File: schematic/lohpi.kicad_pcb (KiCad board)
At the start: 2 copper layers, 0 parts

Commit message: Schematic capture almost done. RF layout started.
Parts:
- added C1: 10uF, Capacitors_SMD:C_0603, F.Cu at (222.2, 74.6)
- added C10: 4.7uF, Capacitors_SMD:C_0603, F.Cu at (226.7, 74.6)
- added C11: 4.7uF, Capacitors_SMD:C_0603, F.Cu at (219.8, 79.6)
- added C12: 4.7uF, Capacitors_SMD:C_0603, F.Cu at (231.4, 69.5)
- added C13: 10nF, Capacitors_SMD:C_0603, F.Cu at (215.3, 86.0)
- added C14: 1.0uF, Capacitors_SMD:C_0603, F.Cu at (219.7, 86.0)
- added C15: 1.0uF, Capacitors_SMD:C_0603, F.Cu at (215.3, 91.1)
- added C16: 1.0uF, Capacitors_SMD:C_0603, F.Cu at (236.1, 69.5)
- added C17: 1.0uF, Capacitors_SMD:C_0603, F.Cu at (231.4, 74.6)
- added C18: 56pF, Capacitors_SMD:C_0603, F.Cu at (200.1, -37.2)
- added C19: 56pF, Capacitors_SMD:C_0603, F.Cu at (163.5, -0.87)
- added C2: 4.7uF, Capacitors_SMD:C_0603, F.Cu at (210.7, 91.1)
- added C20: 56pF, Capacitors_SMD:C_0603, F.Cu at (168.7, -5.92)
- added C21: 56pF, Capacitors_SMD:C_0603, F.Cu at (184.3, -23.1)
- added C22: 56pF, Capacitors_SMD:C_0603, F.Cu at (174.3, -11.0)
- added C23: 56pF, Capacitors_SMD:C_0603, F.Cu at (158.9, 4.18)
- added C24: 1.0uF, Capacitors_SMD:C_0603, F.Cu at (190.2, -30.1)
- added C25: 100nF, Capacitors_SMD:C_0603, F.Cu at (159.3, -16.0)
- added C26: 100nF, Capacitors_SMD:C_0603, F.Cu at (179.7, -23.1)
- added C27: 100nF, Capacitors_SMD:C_0603, F.Cu at (174.8, -16.0)
- added C28: 100nF, Capacitors_SMD:C_0603, F.Cu at (164.5, -16.0)
- added C29: 100nF, Capacitors_SMD:C_0603, F.Cu at (169.7, -16.0)
- added C3: 0.1uF, Capacitors_SMD:C_0603, F.Cu at (206.0, 91.7)
- added C30: 1.0uF, Capacitors_SMD:C_0603, F.Cu at (159.1, -0.87)
- added C31: 100nF, Capacitors_SMD:C_0603, F.Cu at (159.3, -5.92)
- added C32: 100nF, Capacitors_SMD:C_0603, F.Cu at (169.7, -11.0)
- added C33: 100nF, Capacitors_SMD:C_0603, F.Cu at (164.5, -11.0)
- added C34: 1uF, Capacitors_SMD:C_0402, F.Cu at (218.0, 125.9)
- added C35: 1uF, Capacitors_SMD:C_0402, F.Cu at (221.9, 121.3)
- added C36: 100nF, Capacitors_SMD:C_0603, F.Cu at (159.3, -11.0)
- added C37: 4.7uF, Capacitors_SMD:C_0603, F.Cu at (164.3, -5.92)
- added C38: 1nF, Capacitors_SMD:C_0402, F.Cu at (230.3, 111.8)
- added C39: 100nF, Capacitors_SMD:C_0402, F.Cu at (194.9, 116.4)
- added C4: 1nF, Capacitors_SMD:C_0603, F.Cu at (211.5, 86.0)
- added C40: 100nF, Capacitors_SMD:C_0402, F.Cu at (200.1, 107.3)
- added C41: 100nF, Capacitors_SMD:C_0402, F.Cu at (188.5, 126.4)
- added C42: 100nF, Capacitors_SMD:C_0402, F.Cu at (194.9, 111.8)
- added C43: 10nF, Capacitors_SMD:C_0402, F.Cu at (235.6, 102.7)
- added C44: 10nF, Capacitors_SMD:C_0402, F.Cu at (226.5, 111.8)
- added C45: 1uF, Capacitors_SMD:C_0402, F.Cu at (218.4, 121.3)
- added C46: 100nF, Capacitors_SMD:C_0402, F.Cu at (207.2, 102.7)
- added C47: 1uF, Capacitors_SMD:C_0402, F.Cu at (233.1, 107.3)
- added C48: 100nF, Capacitors_SMD:C_0402, F.Cu at (138.3, 153.7)
- added C49: 1uF, Capacitors_SMD:C_0402, F.Cu at (214.4, 126.3)
- added C5: 4.7uF, Capacitors_SMD:C_0603, F.Cu at (206.0, 86.6)
- added C50: 1uF, Capacitors_SMD:C_0402, F.Cu at (229.7, 107.3)
- added C51: DNP, Capacitors_SMD:C_0402, F.Cu at (142.1, 156.8)
- added C52: DNP, Capacitors_SMD:C_0402, F.Cu at (144.7, 156.8)
- added C53: 56pF, Capacitors_SMD:C_0402, F.Cu at (139.6, 160.9)
- added C54: 56pF, Capacitors_SMD:C_0402, F.Cu at (125.7, 153.5)
- added C55: 5.9pF, Capacitors_SMD:C_0402, F.Cu at (123.4, 154.2)
- added C56: 56pF, Capacitors_SMD:C_0402, F.Cu at (129.3, 162.2)
- added C57: DNP, Capacitors_SMD:C_0402, F.Cu at (128.3, 163.8)
- added C58: 56pF, Capacitors_SMD:C_0402, F.Cu at (112.8, 152.7)
- added C59: 2.2uF, Capacitors_SMD:C_0603, F.Cu at (205.0, 107.5)
- added C6: 10nF, Capacitors_SMD:C_0603, F.Cu at (222.2, 69.5)
- added C60: DNP, Capacitors_SMD:C_0402, F.Cu at (126.1, 160.3)
- added C61: 56pF, Capacitors_SMD:C_0402, F.Cu at (257.4, 86.2)
- added C62: 56pF, Capacitors_SMD:C_0402, F.Cu at (221.7, 107.5)
- added C63: 0.1uF, Capacitors_SMD:C_0402, F.Cu at (124.2, 158.2)
- added C64: 10000pF, Capacitors_SMD:C_0402, F.Cu at (195.9, 102.7)
- added C65: 56pF, Capacitors_SMD:C_0402, F.Cu at (123.1, 156.7)
- added C66: 2.2uF, Capacitors_SMD:C_0603, F.Cu at (212.1, 102.9)
- added C67: 2.2uF, Capacitors_SMD:C_0603, F.Cu at (193.9, 122.0)
- added C68: 56pF, Capacitors_SMD:C_0402, F.Cu at (105.3, 151.0)
- added C69: 56pF, Capacitors_SMD:C_0402, F.Cu at (214.6, 117.2)
- added C7: 1.0uF, Capacitors_SMD:C_0603, F.Cu at (192.5, 94.7)
- added C70: 56pF, Capacitors_SMD:C_0402, F.Cu at (206.0, 126.6)
- added C71: 56pF, Capacitors_SMD:C_0402, F.Cu at (210.4, 117.4)
- added C72: DNP, Capacitors_SMD:C_0402, F.Cu at (116.8, 162.3)
- added C73: 56pF, Capacitors_SMD:C_0402, F.Cu at (201.7, 126.6)
- added C74: 5.6pF, Capacitors_SMD:C_0402, F.Cu at (113.7, 163.1)
- added C75: 56pF, Capacitors_SMD:C_0402, F.Cu at (112.4, 160.9)
- added C76: 56pF, Capacitors_SMD:C_0402, F.Cu at (103.8, 158.1)
- added C77: 56pF, Capacitors_SMD:C_0402, F.Cu at (101.1, 153.9)
- added C78: 0.01uF, Capacitors_SMD:C_0402, F.Cu at (188.7, 121.8)
- added C79: 1nF, Capacitors_SMD:C_0603, F.Cu at (179.1, -18.0)
- added C8: 10uF, Capacitors_SMD:C_0603, F.Cu at (188.0, 94.7)
- added C80: 100nF, Capacitors_SMD:C_0402, F.Cu at (202.0, 102.7)
- added C9: 4.7uF, Capacitors_SMD:C_0603, F.Cu at (226.7, 69.5)
- added D1: LED, LEDs:LED_0603, F.Cu at (189.4, -15.3)
- added D2: LED, LEDs:LED_0603, F.Cu at (179.4, -8.22)
- added D3: LED, LEDs:LED_0603, F.Cu at (174.4, -1.17)
- added D4: LED, LEDs:LED_0603, F.Cu at (210.9, -37.4)
- added J1: CONN_01X02, Pin_Headers:Pin_Header_Straight_1x02_Pitch2.54mm, F.Cu at (207.5, 70.3)
- added J10: CONN_01X01, rpi_mounting_hole:rpi_mounting_hole, F.Cu at (77.3, -0.25)
- added J11: CONN_01X01, rpi_mounting_hole:rpi_mounting_hole, F.Cu at (77.0, 48.0)
- added J12: CONN_01X01, rpi_mounting_hole:rpi_mounting_hole, F.Cu at (134.6, -0.38)
- added J13: CONN_01X01, rpi_mounting_hole:rpi_mounting_hole, F.Cu at (135.1, 48.0)
- added J2: CONN_01X01, SMD_Packages:1Pin, F.Cu at (315.1, 71.5)
- added J3: CONN_01X01, SMD_Packages:1Pin, F.Cu at (294.7, 71.5)
- added J4: CONN_01X01, SMD_Packages:1Pin, F.Cu at (294.7, 80.8)
- added J5: CONN_01X01, SMD_Packages:1Pin, F.Cu at (304.9, 71.5)
- added J6: CONN_01X01, SMD_Packages:1Pin, F.Cu at (304.9, 80.8)
- added J7: CONN_01X05, Pin_Headers:Pin_Header_Straight_1x05_Pitch2.54mm, F.Cu at (161.9, -36.3)
- added J8: raspberry_pi_3_header, Socket_Strips:Socket_Strip_Straight_2x20_Pitch2.54mm, B.Cu at (81.8, 0.76)
- added J9: CONN_01X02, Connectors_Molex:Molex_SMA_Jack_Edge_Mount, F.Cu at (93.1, 153.9)
- added L2: 33uH, Inductors_SMD:L_0402, F.Cu at (276.1, 105.1)
- added L3: 3.9uH, Inductors_SMD:L_0402, F.Cu at (128.1, 153.5)
- added L4: 8.2nH, Inductors_SMD:L_0402, F.Cu at (127.8, 160.9)
- added L5: L, Inductors_SMD:L_0402, F.Cu at (110.9, 153.2)
- added L6: 6.8nH, Inductors_SMD:L_0603, F.Cu at (263.6, 101.3)
- added L7: 18nH, Inductors_SMD:L_0603, F.Cu at (115.7, 158.4)
- added L8: 2.7nH, Inductors_SMD:L_0402, F.Cu at (115.2, 160.9)
- added Q1: Q_PMOS_GSD, TO_SOT_Packages_SMD:SOT-23, F.Cu at (191.0, 88.6)
- added Q2: NXP 2N7002, TO_SOT_Packages_SMD:SOT-23, F.Cu at (182.8, -36.2)
- added Q3: NXP 2N7002, TO_SOT_Packages_SMD:SOT-23, F.Cu at (192.9, -36.2)
- added Q4: NXP 2N7002, TO_SOT_Packages_SMD:SOT-23, F.Cu at (182.8, -29.1)
- added Q5: NXP 2N7002, TO_SOT_Packages_SMD:SOT-23, F.Cu at (172.0, -22.1)
- added R1: 10, Resistors_SMD:R_0603, F.Cu at (223.6, 79.6)
- added R10: 0, Resistors_SMD:R_0603, F.Cu at (232.1, 84.6)
- added R11: 0, Resistors_SMD:R_0603, F.Cu at (226.8, 79.6)
- added R12: 0, Resistors_SMD:R_0603, F.Cu at (264.7, 89.4)
- added R13: 100, Resistors_SMD:R_0603, F.Cu at (176.0, -5.97)
- added R14: 100, Resistors_SMD:R_0603, F.Cu at (203.9, -32.2)
- added R15: 100, Resistors_SMD:R_0603, F.Cu at (158.5, 14.2)
- added R16: DNP, Resistors_SMD:R_0603, F.Cu at (167.4, -0.92)
- added R17: DNP, Resistors_SMD:R_0603, F.Cu at (193.1, -25.1)
- added R18: DNP, Resistors_SMD:R_0603, F.Cu at (158.5, 9.18)
- added R19: DNP, Resistors_SMD:R_0603, F.Cu at (189.5, -20.1)
- added R2: 24.9k, Resistors_SMD:R_0603, F.Cu at (224.4, 84.6)
- added R20: DNP, Resistors_SMD:R_0603, F.Cu at (197.8, -27.2)
- added R21: 100, Resistors_SMD:R_0603, F.Cu at (162.1, 9.18)
- added R22: 330, Resistors_SMD:R_0603, F.Cu at (171.0, -0.92)
- added R23: 330, Resistors_SMD:R_0603, F.Cu at (167.4, 4.08)
- added R24: 10k, Resistors_SMD:R_0603, F.Cu at (186.0, -18.1)
- added R25: 100, Resistors_SMD:R_0603, F.Cu at (182.6, -13.1)
- added R26: 330, Resistors_SMD:R_0603, F.Cu at (186.0, -13.1)
- added R27: 100, Resistors_SMD:R_0603, F.Cu at (193.1, -20.1)
- added R28: 330, Resistors_SMD:R_0603, F.Cu at (207.5, -37.2)
- added R29: 100, Resistors_SMD:R_0603, F.Cu at (194.2, -30.2)
- added R3: 10k, Resistors_SMD:R_0603, F.Cu at (235.3, 74.5)
- added R30: 100, Resistors_SMD:R_0603, F.Cu at (189.6, -25.1)
- added R31: 100, Resistors_SMD:R_0603, F.Cu at (128.7, 39.4)
- added R32: 100, Resistors_SMD:R_0603, F.Cu at (182.6, -18.1)
- added R33: 100, Resistors_SMD:R_0603, F.Cu at (179.1, -13.0)
- added R34: 100, Resistors_SMD:R_0603, F.Cu at (162.7, 4.13)
- added R35: 100, Resistors_SMD:R_0603, F.Cu at (172.5, -5.97)
- added R36: DNP, Resistors_SMD:R_0603, F.Cu at (204.0, -37.2)
- added R37: 0, Resistors_SMD:R_0402, F.Cu at (142.7, 155.4)
- added R38: 0, Resistors_SMD:R_0402, F.Cu at (144.0, 155.4)
- added R39: 150, Resistors_SMD:R_0402, F.Cu at (132.7, 161.4)
- added R4: 0, Resistors_SMD:R_0603, F.Cu at (219.2, 91.0)
- added R40: 36.5, Resistors_SMD:R_0402, F.Cu at (131.2, 160.9)
- added R41: 150, Resistors_SMD:R_0402, F.Cu at (129.8, 160.4)
- added R42: DNP, Resistors_SMD:R_0402, F.Cu at (116.7, 152.1)
- added R43: 500, Resistors_SMD:R_0402, F.Cu at (114.9, 152.7)
- added R44: 49.9, Resistors_SMD:R_0402, F.Cu at (193.0, 126.9)
- added R45: DNP, Resistors_SMD:R_0402, F.Cu at (114.3, 154.2)
- added R46: 36.5, Resistors_SMD:R_0402, F.Cu at (125.1, 156.7)
- added R47: 3.9, Resistors_SMD:R_0402, F.Cu at (199.2, 116.8)
- added R48: 300, Resistors_SMD:R_0402, F.Cu at (199.2, 111.9)
- added R49: 300, Resistors_SMD:R_0402, F.Cu at (213.6, 107.8)
- added R5: DNP, Resistors_SMD:R_0603, F.Cu at (228.6, 84.6)
- added R6: 0, Resistors_SMD:R_0603, F.Cu at (222.1, 91.0)
- added R7: 30.9k, Resistors_SMD:R_0603, F.Cu at (234.3, 79.6)
- added R8: 24.9k, Resistors_SMD:R_0603, F.Cu at (225.9, 89.6)
- added R9: 0, Resistors_SMD:R_0603, F.Cu at (238.1, 79.5)
- added REF**: Pin_Header_Straight_1x04_Pitch2.00mm, Pin_Headers:Pin_Header_Straight_1x04_Pitch2.00mm, F.Cu at (149.5, 151.8)
- added U1: MCP1726-3302E/SN, Housings_SOIC:SOIC-8_3.9x4.9mm_Pitch1.27mm, F.Cu at (194.2, 71.5)
- added U10: Anaren_B0430J50100AHF, anaren_balun:anaren_balun, F.Cu at (143.5, 158.5)
- added U11: MurataSF2314E, murata_saw_filter:murata_saw_filter, F.Cu at (136.4, 160.9)
- added U12: MurataSF2314E, murata_saw_filter:murata_saw_filter, F.Cu at (120.3, 153.5)
- added U13: SPF5043Z, quorvo:quorvo_spf5043z, F.Cu at (108.5, 151.6)
- added U14: RFPA0133TR7, Housings_DFN_QFN:QFN-16-1EP_3x3mm_Pitch0.5mm, F.Cu at (123.3, 161.2)
- added U15: MurataSF2314E, murata_saw_filter:murata_saw_filter, F.Cu at (106.8, 160.9)
- added U16: RFSW1012, quorvo:rfsw1012DS, F.Cu at (103.8, 153.9)
- added U17: MurataSF2314E, murata_saw_filter:murata_saw_filter, F.Cu at (98.0, 153.9)
- added U2: MCP1612, Housings_SSOP:MSOP-8_3x3mm_Pitch0.65mm, F.Cu at (213.7, 79.9)
- added U3: MCP1726-3302E/SN, Housings_SOIC:SOIC-8_3.9x4.9mm_Pitch1.27mm, F.Cu at (194.2, 80.6)
- added U4: MCP1824, TO_SOT_Packages_SMD:SOT-23-5, F.Cu at (206.2, 80.2)
- added U5: MCP1824, TO_SOT_Packages_SMD:SOT-23-5, F.Cu at (199.9, 89.0)
- added U6: MCP1824, TO_SOT_Packages_SMD:SOT-23-5, F.Cu at (216.4, 70.9)
- added U7: SX1301, Housings_DFN_QFN:QFN-64-1EP_9x9mm_Pitch0.5mm, F.Cu at (124.8, 13.3)
- added U8: SX1257, Housings_DFN_QFN:QFN-32-1EP_5x5mm_Pitch0.5mm, F.Cu at (130.9, 148.6)
- added U9: SX1257, Housings_DFN_QFN:QFN-32-1EP_5x5mm_Pitch0.5mm, F.Cu at (142.9, 148.6)
- added X1: ABRACON-OSC, crystal_osc_1:ABRACON-OSC, F.Cu at (246.3, 92.1)
- added X2: ABRACON-OSC, crystal_osc_1:ABRACON-OSC, F.Cu at (255.4, 101.6)
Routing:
- net GND: track 0.00 -> 123.0 mm, vias 0 -> 5
- net Net-(L2-Pad2): track 0.00 -> 17.1 mm
- net Net-(C72-Pad1): track 0.00 -> 10.9 mm
- net Net-(J9-Pad1): track 0.00 -> 5.60 mm
- net Net-(C53-Pad1): track 0.00 -> 4.56 mm
- net Net-(R42-Pad2): track 0.00 -> 4.23 mm
- net Net-(R37-Pad2): track 0.00 -> 4.19 mm
- net Net-(R38-Pad2): track 0.00 -> 4.17 mm
- net Net-(C63-Pad1): track 0.00 -> 4.06 mm
- net Net-(C75-Pad1): track 0.00 -> 3.96 mm
- net Net-(C54-Pad1): track 0.00 -> 3.91 mm
- net Net-(R39-Pad1): track 0.00 -> 3.69 mm
- net Net-(C74-Pad1): track 0.00 -> 3.52 mm
- net Net-(C76-Pad1): track 0.00 -> 3.47 mm
- net Net-(C58-Pad1): track 0.00 -> 3.08 mm
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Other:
- board outline added: 65 x 56 mm
- copper layers 2 -> 4
- net class Default: clearance 0.2 -> 0.14
- net class rf_50_ohm added: clearance 0.12, trace_width 0.36, via_dia 0.8, via_drill 0.4
- rule trace_clearance: 0.2 -> 0.14

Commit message: RF layout updated. Rest still needs work
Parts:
- removed Q2, Q3, Q4, Q5: NXP 2N7002, TO_SOT_Packages_SMD:SOT-23
- removed REF**: Pin_Header_Straight_1x04_Pitch2.00mm, Pin_Headers:Pin_Header_Straight_1x04_Pitch2.00mm
- added C81: 1.5pF, Capacitors_SMD:C_0402_NoSilk, F.Cu at (129.4, 147.1)
- added L1: 3.3uH, Inductors_SMD:L_0603, F.Cu at (129.3, 123.2)
- added R50: 30, Resistors_SMD:R_0402_NoSilk, F.Cu at (126.5, 148.8)
- C1, C10, C12, C2, C22, C23, C33, C9, R25, R27, R29, R30, R31, R32, R33, R34, R35, R36: moved to B.Cu
- C34, C45, C49: footprint Capacitors_SMD:C_0402 -> Capacitors_SMD:C_0402_NoSilk; moved to B.Cu
- C35, C38, C39, C40, C41, C42, C43, C44, C46, C47, C48, C50, C51, C52, C53, C54, C56, C57, C58, C60, C61, C62, C63, C64, C65, C68, C69, C70, C71, C72, C73, C74, C75, C76, C77, C78, C80: footprint Capacitors_SMD:C_0402 -> Capacitors_SMD:C_0402_NoSilk
- C36, C59, C66, C67: footprint Capacitors_SMD:C_0603 -> Capacitors_SMD:C_0402_NoSilk
- C55: value 5.9pF -> 1.5pF; footprint Capacitors_SMD:C_0402 -> Capacitors_SMD:C_0402_NoSilk
- J9: footprint Connectors_Molex:Molex_SMA_Jack_Edge_Mount -> Connectors:SMA_THT_Jack_Straight
- L2: value 33uH -> 1.5nH
- L3: value 3.9uH -> 1.5nH
- L6, L7: footprint Inductors_SMD:L_0603 -> Inductors_SMD:L_0402
- R37, R38, R39, R40, R41, R42, R43, R44, R45, R46, R47, R48, R49: footprint Resistors_SMD:R_0402 -> Resistors_SMD:R_0402_NoSilk
- moved D4 206.5 mm to (92.6, 131.8)
- moved R28 202.0 mm to (96.9, 131.8), turned to 180 degrees
- moved R27 187.7 mm to (103.4, 144.8), turned to 270 degrees
- moved J7 182.3 mm to (84.6, 128.8)
- moved R36 180.4 mm to (145.2, 133.3), turned to 90 degrees
- moved R20 179.6 mm to (98.4, 122.4), turned to 90 degrees
- moved R17 177.8 mm to (93.9, 122.4), turned to 90 degrees
- moved R25 175.2 mm to (111.0, 146.8), turned to 270 degrees
- moved C24 175.1 mm to (120.9, 130.7)
- moved C18 174.1 mm to (126.0, 120.4), turned to 90 degrees
- moved C22 173.6 mm to (112.3, 151.1)
- moved R14 173.4 mm to (121.4, 120.3), turned to 90 degrees
- moved D1 172.0 mm to (92.6, 126.9)
- moved C79 171.5 mm to (112.0, 139.8), turned to 270 degrees
- moved R29 171.1 mm to (143.9, 133.3), turned to 90 degrees
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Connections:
- net /main_receiver/RADIO_C_CLK_OUT renamed /main_receiver/SP_CLK_IN
- C24 pad 2: Net-(C24-Pad2) -> GND
- C25 pad 2: Net-(C24-Pad2) -> GND
- C26 pad 2: Net-(C24-Pad2) -> GND
- C27 pad 2: Net-(C24-Pad2) -> GND
- C28 pad 2: Net-(C24-Pad2) -> GND
- C29 pad 2: Net-(C24-Pad2) -> GND
- C30 pad 2: Net-(C30-Pad2) -> GND
- C31 pad 2: Net-(C30-Pad2) -> GND
- C32 pad 2: Net-(C30-Pad2) -> GND
- C33 pad 2: Net-(C30-Pad2) -> GND
- C36 pad 2: Net-(C24-Pad2) -> GND
- C37 pad 2: Net-(C24-Pad2) -> GND
- C55 pad 1: Net-(C54-Pad1) -> GND
- C55 pad 2: GND -> Net-(C55-Pad2)
- C78 pad 2: +3V3 -> /power_supply/VCC_RADIO_A
- C79 pad 2: Net-(C24-Pad2) -> GND
- D1 pad 1: Net-(D1-Pad1) -> GND
- D2 pad 1: Net-(D2-Pad1) -> GND
- D3 pad 1: Net-(D3-Pad1) -> GND
- D4 pad 1: Net-(D4-Pad1) -> GND
- J10 pad 1: Net-(J10-Pad1) -> (no net)
- J11 pad 1: Net-(J11-Pad1) -> (no net)
- J12 pad 1: Net-(J12-Pad1) -> (no net)
- J13 pad 1: Net-(J13-Pad1) -> (no net)
- J8 pad 1: (no net) -> Net-(J8-Pad1)
- J8 pad 10: (no net) -> Net-(J8-Pad10)
- J8 pad 12: (no net) -> Net-(J8-Pad12)
- J8 pad 16: (no net) -> Net-(J8-Pad16)
- J8 pad 17: (no net) -> Net-(J8-Pad17)
- J8 pad 18: (no net) -> Net-(J8-Pad18)
- J8 pad 22: (no net) -> Net-(J8-Pad22)
- J8 pad 24: (no net) -> Net-(J8-Pad24)
- J8 pad 26: (no net) -> Net-(J8-Pad26)
- J8 pad 27: (no net) -> Net-(J8-Pad27)
- J8 pad 28: (no net) -> Net-(J8-Pad28)
- J8 pad 3: (no net) -> Net-(J8-Pad3)
- J8 pad 32: (no net) -> Net-(J8-Pad32)
- J8 pad 33: (no net) -> Net-(J8-Pad33)
- J8 pad 35: (no net) -> Net-(J8-Pad35)
- J8 pad 36: (no net) -> Net-(J8-Pad36)
- J8 pad 37: (no net) -> Net-(J8-Pad37)
- J8 pad 38: (no net) -> Net-(J8-Pad38)
- J8 pad 40: (no net) -> Net-(J8-Pad40)
- J8 pad 5: (no net) -> Net-(J8-Pad5)
- J8 pad 7: (no net) -> Net-(J8-Pad7)
- J8 pad 8: (no net) -> Net-(J8-Pad8)
- L2 pad 1: GND -> Net-(C55-Pad2)
- L2 pad 2: Net-(L2-Pad2) -> Net-(C54-Pad2)
- L3 pad 1: Net-(L2-Pad2) -> Net-(C54-Pad2)
- L3 pad 2: Net-(C54-Pad2) -> Net-(C81-Pad1)
- R22 pad 1: +3V3 -> /main_receiver/GPIO[0]
- R23 pad 1: +3V3 -> /main_receiver/GPIO[1]
- R26 pad 1: +3V3 -> /main_receiver/GPIO[2]
- R28 pad 1: +3V3 -> /main_receiver/GPIO[3]
- U1 pad 5: (no net) -> Net-(U1-Pad5)
- U10 pad 5: Net-(U10-Pad5) -> (no net)
- U14 pad 1: Net-(U14-Pad1) -> (no net)
- U14 pad 11: Net-(U14-Pad11) -> (no net)
- U14 pad 15: Net-(U14-Pad15) -> (no net)
- U14 pad 4: Net-(U14-Pad4) -> (no net)
- U14 pad 5: Net-(U14-Pad5) -> (no net)
- U14 pad 7: Net-(U14-Pad7) -> (no net)
- U14 pad 8: Net-(U14-Pad8) -> (no net)
- U16 pad 9: +3V3 -> /power_supply/VCC_RADIO_A
- U2 pad 8: (no net) -> Net-(L1-Pad1)
- U3 pad 5: (no net) -> Net-(U3-Pad5)
- U4 pad 4: (no net) -> Net-(U4-Pad4)
- U5 pad 4: (no net) -> Net-(U5-Pad4)
- U6 pad 4: (no net) -> Net-(U6-Pad4)
- U7 pad 26: (no net) -> Net-(U7-Pad26)
- U7 pad 27: (no net) -> Net-(U7-Pad27)
- U7 pad 37: (no net) -> Net-(U7-Pad37)
- U7 pad 38: (no net) -> Net-(U7-Pad38)
- U7 pad 9: (no net) -> Net-(U7-Pad9)
- U8 pad 11: (no net) -> Net-(U8-Pad11)
- U8 pad 21: (no net) -> Net-(U8-Pad21)
- U8 pad 22: (no net) -> Net-(U8-Pad22)
- U8 pad 23: (no net) -> Net-(U8-Pad23)
- U8 pad 24: (no net) -> Net-(U8-Pad24)
- U8 pad 27: Net-(L2-Pad2) -> Net-(C81-Pad1)
- U8 pad 29: (no net) -> Net-(U8-Pad29)
- U8 pad 30: (no net) -> Net-(U8-Pad30)
- U8 pad 6: (no net) -> Net-(U8-Pad6)
- U9 pad 21: (no net) -> Net-(U9-Pad21)
- U9 pad 22: (no net) -> Net-(U9-Pad22)
- U9 pad 23: (no net) -> Net-(U9-Pad23)
- U9 pad 24: (no net) -> Net-(U9-Pad24)
- U9 pad 27: Net-(L2-Pad2) -> Net-(C55-Pad2)
- U9 pad 6: (no net) -> Net-(U9-Pad6)
- X2 pad 1: Net-(X2-Pad1) -> (no net)
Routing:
- net /main_receiver/SP_CLK_IN: track 0.00 -> 69.6 mm, vias 0 -> 3
- net /main_receiver/PA_A_EN: track 0.00 -> 64.2 mm, vias 0 -> 3
- net Net-(R35-Pad2): track 0.00 -> 63.2 mm, vias 0 -> 1
- net Net-(R29-Pad2): track 0.00 -> 61.7 mm, vias 0 -> 1
- net Net-(R30-Pad2): track 0.00 -> 58.9 mm, vias 0 -> 1
- net Net-(R31-Pad2): track 0.00 -> 55.5 mm, vias 0 -> 1
- net /main_receiver/RPI_5v: track 0.00 -> 52.6 mm, vias 0 -> 1
- net Net-(R32-Pad2): track 0.00 -> 52.1 mm, vias 0 -> 1
- net /main_receiver/PA_G8: track 0.00 -> 51.9 mm, vias 0 -> 1
- net /main_receiver/PA_G16: track 0.00 -> 51.6 mm, vias 0 -> 1
- net GND: track 123.0 -> 168.3 mm, vias 5 -> 43
- net /main_receiver/RPI_SS4: track 0.00 -> 44.2 mm, vias 0 -> 1
- net /main_receiver/RPI_SS5: track 0.00 -> 42.0 mm, vias 0 -> 1
- net /main_receiver/RADIO_B_EN: track 0.00 -> 39.5 mm, vias 0 -> 3
- net Net-(R27-Pad1): track 0.00 -> 38.3 mm, vias 0 -> 1
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- added copper zone on In2.Cu, net +5V
- added copper zone on F.Cu, net GND
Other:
- net class rf_50_ohm removed

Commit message: PCB layout finished, needs review
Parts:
- removed J7: CONN_01X05, Pin_Headers:Pin_Header_Straight_1x05_Pitch2.54mm
- added C84: 1.0uF, Capacitors_SMD:C_0603, F.Cu at (138.2, 135.1)
- added C85: 1.0uF, Capacitors_SMD:C_0603, F.Cu at (119.8, 138.3)
- added C86: 1.0uF, Capacitors_SMD:C_0603, F.Cu at (107.2, 145.3)
- added C87: 1.0uF, Capacitors_SMD:C_0603, F.Cu at (130.7, 160.3)
- added C89: 1.0uF, Capacitors_SMD:C_0603, F.Cu at (125.0, 136.0)
- added C90: 1.0uF, Capacitors_SMD:C_0603, F.Cu at (112.4, 146.6)
- added C91: 1.0uF, Capacitors_SMD:C_0603, F.Cu at (119.1, 159.1)
- added L10: 2.2uH, Inductors_SMD:L_0805, F.Cu at (128.5, 162.1)
- added L11: 2.2uH, Inductors_SMD:L_0805, F.Cu at (135.3, 134.1)
- added L12: 2.2uH, Inductors_SMD:L_0805, F.Cu at (122.9, 138.2)
- added L13: 2.2uH, Inductors_SMD:L_0805, F.Cu at (110.1, 144.0)
- added L9: 2.2uH, Inductors_SMD:L_0805, F.Cu at (129.0, 131.2)
- C1, C10, C12, C2, C22, C23, C33, C34, C45, C49, C9, R25, R27, R29, R30, R31, R32, R33, R34, R35, R36: moved to F.Cu
- J2, J3, J4, J5, J6: footprint SMD_Packages:1Pin -> Pin_Headers:Pin_Header_Straight_1x01_Pitch2.54mm
- moved J6 212.7 mm to (100.8, 140.8)
- moved J5 199.8 mm to (118.7, 144.1)
- moved J3 186.0 mm to (132.3, 164.6)
- moved J2 183.3 mm to (142.2, 132.6)
- moved J4 164.5 mm to (138.6, 132.6)
- moved C1 61.9 mm to (98.2, 144.5)
- moved C9 61.0 mm to (96.5, 144.5)
- moved C2 45.9 mm to (114.2, 141.8), turned to 270 degrees
- moved C45 34.1 mm to (127.3, 137.0)
- moved C12 33.0 mm to (125.2, 133.5), turned to 270 degrees
- moved R35 31.4 mm to (130.9, 136.8)
- moved C10 27.9 mm to (140.1, 124.5), turned to 0 degrees
- moved C33 27.2 mm to (125.6, 131.3), turned to 180 degrees
- moved C34 27.2 mm to (131.6, 146.9), turned to 270 degrees
- moved C49 25.1 mm to (133.6, 145.0), turned to 270 degrees
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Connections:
- R10 pad 1: /power_supply/VCC_RADIO_A -> Net-(C84-Pad1)
- R11 pad 1: /power_supply/VCC_RADIO_B -> Net-(C85-Pad1)
- R12 pad 1: /power_supply/VCC_LNA_A -> Net-(C86-Pad1)
- R6 pad 1: +3V3 -> Net-(L9-Pad1)
- R9 pad 1: /power_supply/VCC_PA -> Net-(C87-Pad1)
- U7 pad 54: /main_receiver/GPIO[4] -> (no net)
- U8 pad 33: (no net) -> GND
- U9 pad 33: (no net) -> GND
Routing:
- net GND: track 168.3 -> 349.2 mm, vias 43 -> 119
- net +1V8: track 32.8 -> 83.0 mm, vias 3 -> 6
- net /main_receiver/A_SCKL: track 4.83 -> 49.3 mm, vias 1 -> 2
- net /main_receiver/A_MOSI: track 3.04 -> 47.0 mm, vias 1 -> 2
- net /main_receiver/A_MISO: track 3.88 -> 47.7 mm, vias 1 -> 2
- net /main_receiver/A_NSS: track 2.20 -> 45.9 mm, vias 1 -> 2
- net /power_supply/VCC_RADIO_A: track 32.7 -> 76.0 mm, vias 5 -> 6
- net Net-(R29-Pad2): track 61.7 -> 19.4 mm, vias 1 -> 0
- net Net-(R30-Pad2): track 58.9 -> 19.2 mm, vias 1 -> 0
- net Net-(R31-Pad2): track 55.5 -> 19.4 mm, vias 1 -> 0
- net Net-(R32-Pad2): track 52.1 -> 19.9 mm, vias 1 -> 0
- net /main_receiver/SCLK: track 3.96 -> 34.5 mm, vias 1 -> 2
- net Net-(R35-Pad2): track 63.2 -> 34.9 mm, vias 1 -> 2
- net /main_receiver/SP_CLK_IN: track 69.6 -> 42.0 mm, vias 3 -> 2
- net /main_receiver/MISO: track 3.93 -> 30.1 mm, vias 1 -> 2
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- added copper zone on B.Cu, net GND
- added copper zone on In1.Cu, net GND

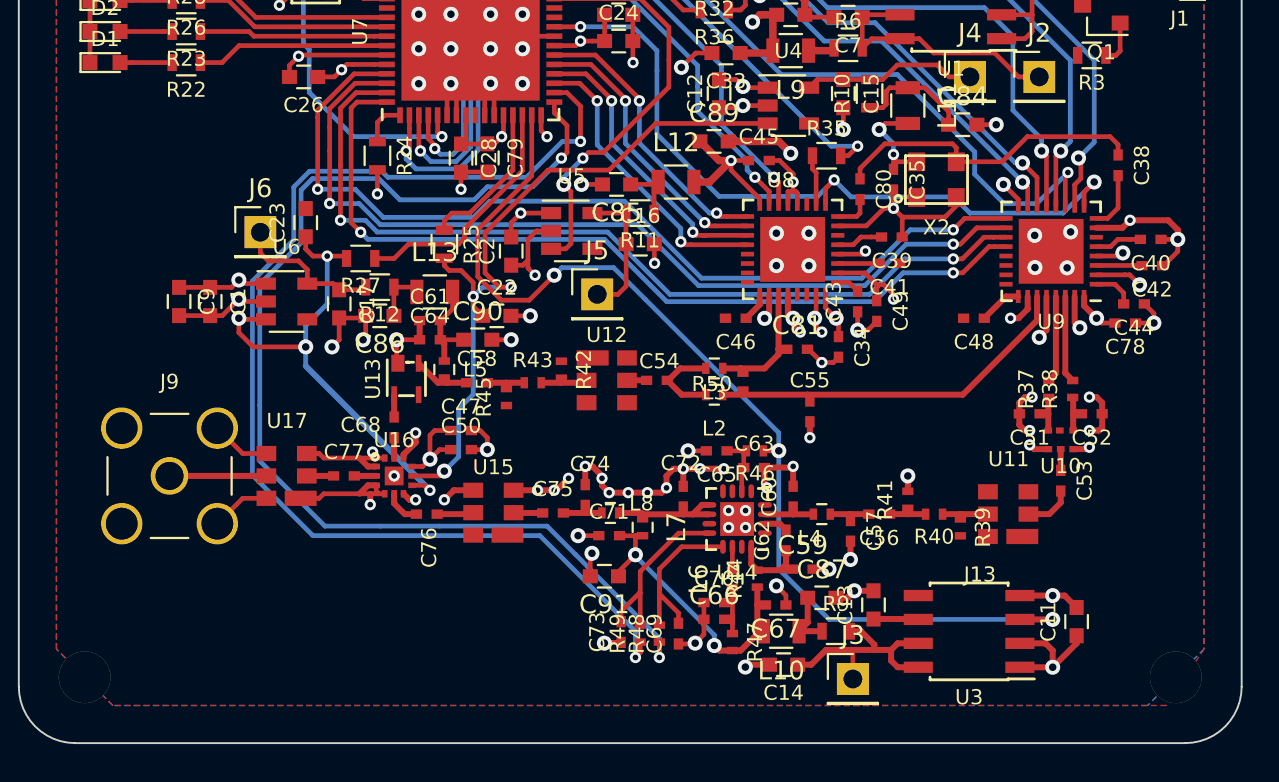
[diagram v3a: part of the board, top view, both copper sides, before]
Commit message: Adds via stitching, better ground infill.
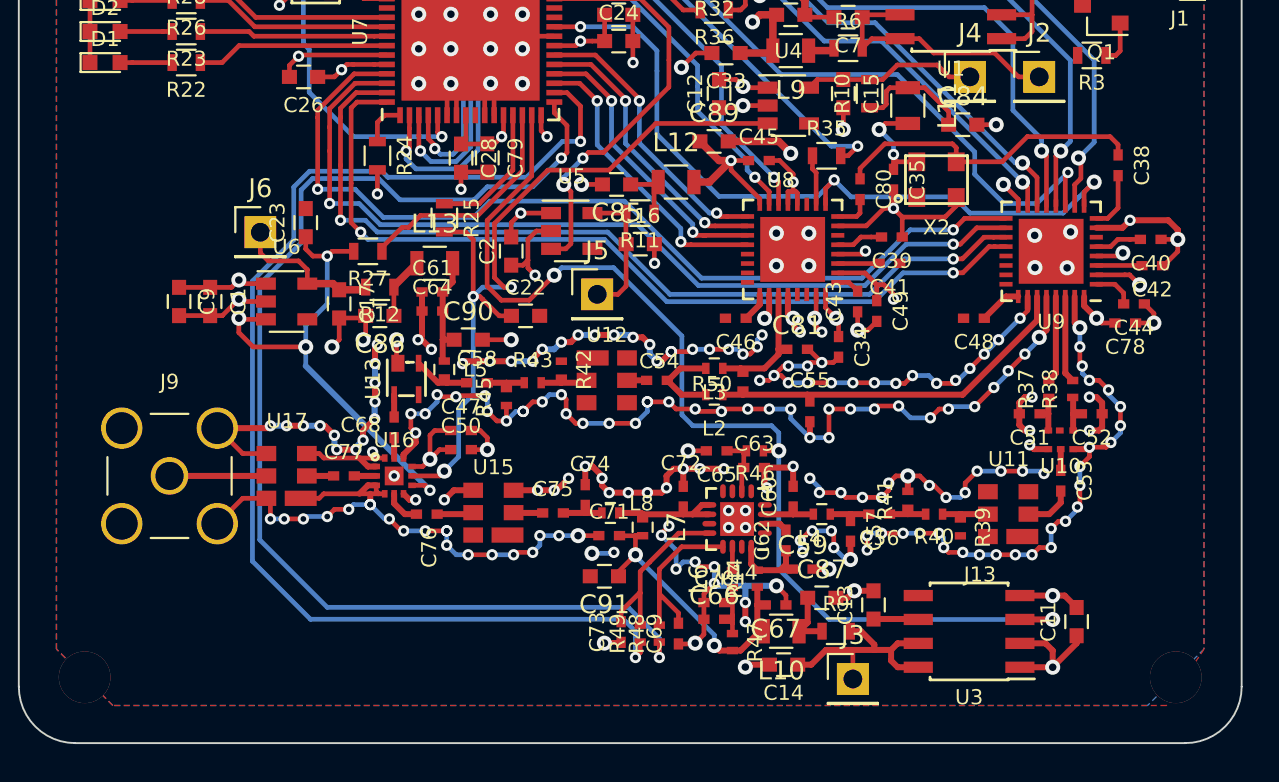
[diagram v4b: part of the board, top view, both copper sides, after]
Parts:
- moved C61 1.53 mm to (110.0, 144.0)
- moved C64 1.53 mm to (110.0, 145.0)
- moved C22 1.52 mm to (114.9, 145.3)
- moved L13 1.52 mm to (110.1, 142.5)
- moved R25 1.40 mm to (110.6, 140.1)
- moved R27 0.54 mm to (106.6, 141.9)
- moved C90 0.51 mm to (111.9, 146.6)
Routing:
- net GND: track 349.2 -> 525.2 mm, vias 119 -> 273
- net /power_supply/VCC_RADIO_A: track 76.0 -> 53.4 mm
- net /main_receiver/PA_G8: track 62.4 -> 65.1 mm
- net /main_receiver/PA_G16: track 61.2 -> 63.6 mm
- net /main_receiver/RADIO_A_EN: track 39.5 -> 41.9 mm
- net /main_receiver/PA_A_EN: track 56.1 -> 58.2 mm
- net /power_supply/VCC_LNA_A: track 5.00 -> 6.05 mm
- net Net-(R25-Pad1): track 8.17 -> 7.30 mm
- net Net-(R27-Pad1): track 13.0 -> 12.3 mm
